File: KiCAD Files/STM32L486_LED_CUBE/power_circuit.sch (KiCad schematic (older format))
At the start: 21 parts

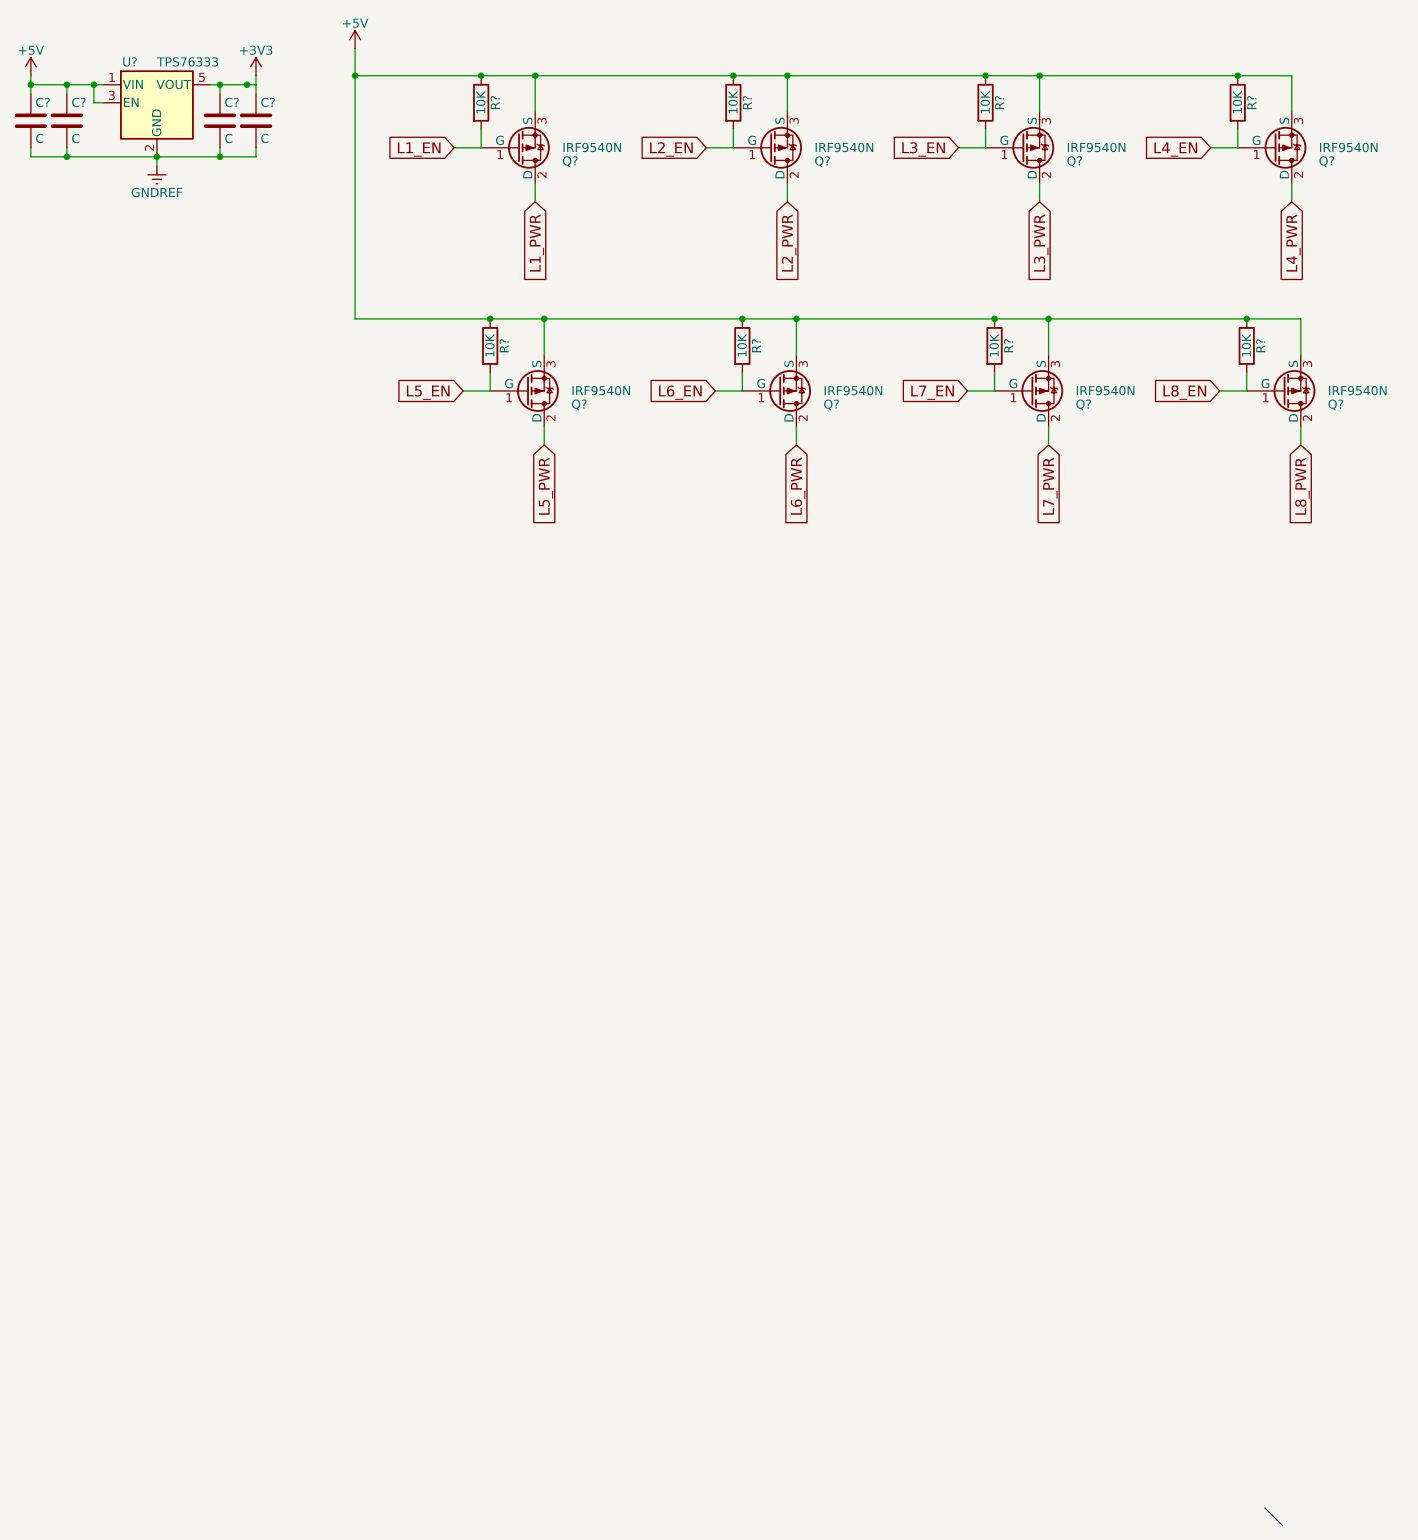
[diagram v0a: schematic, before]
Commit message: Updated KiCAD schematic. TLC portion added.
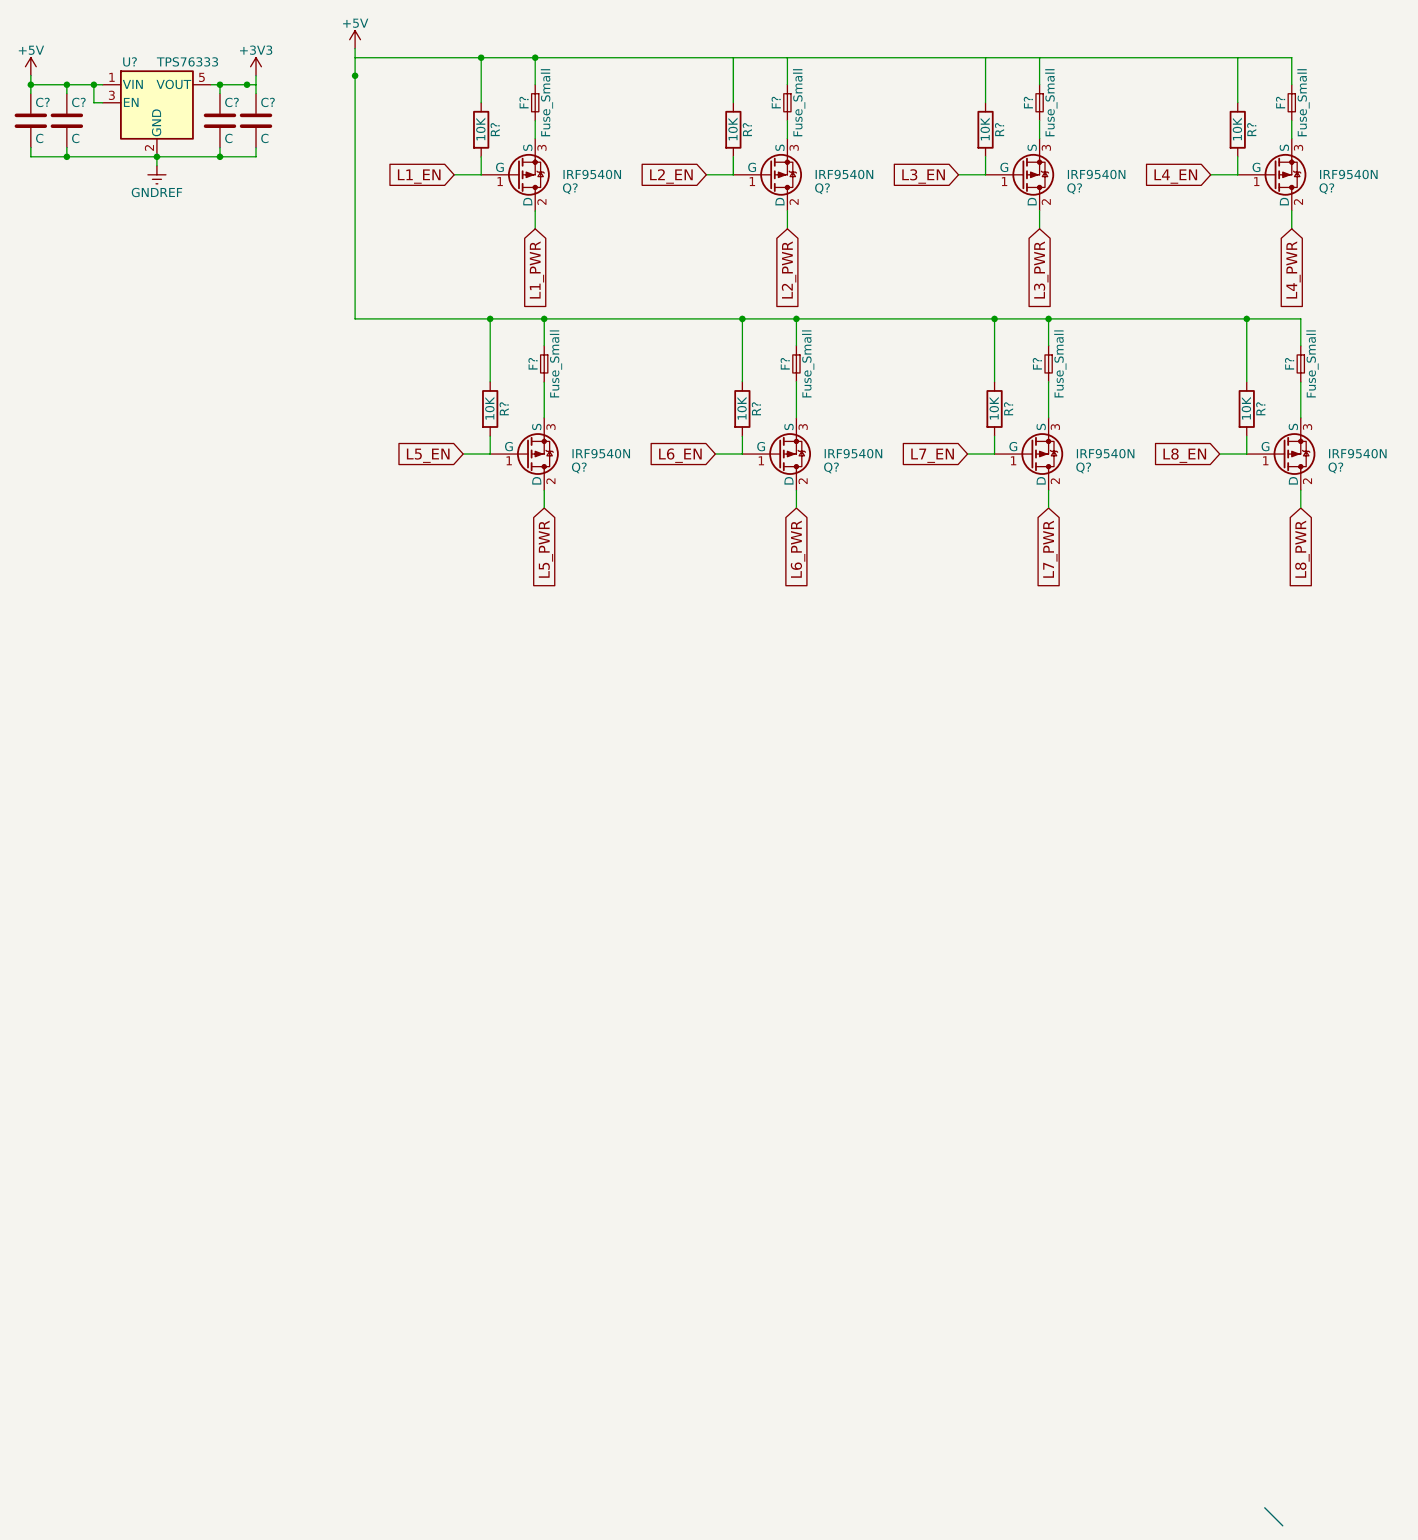
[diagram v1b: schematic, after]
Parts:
- removed Q? (x3): IRF9540N, TO_SOT_Packages_THT:TO-220_Vertical, symbol IRF9540N
- removed R? (x3): 10K, symbol R
- added F? (x8): Fuse_Small, symbol Fuse_Small
- added Q? (x3): IRF9540N, TO_SOT_Packages_THT:TO-220_Vertical, symbol IRF9540N
- added R? (x3): 10K, symbol R
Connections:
- wire segments 49 -> 83
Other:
- moved on the sheet: Q?, R?
